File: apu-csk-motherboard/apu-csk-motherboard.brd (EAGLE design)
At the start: 90.2 x 95.9 mm, 11 parts

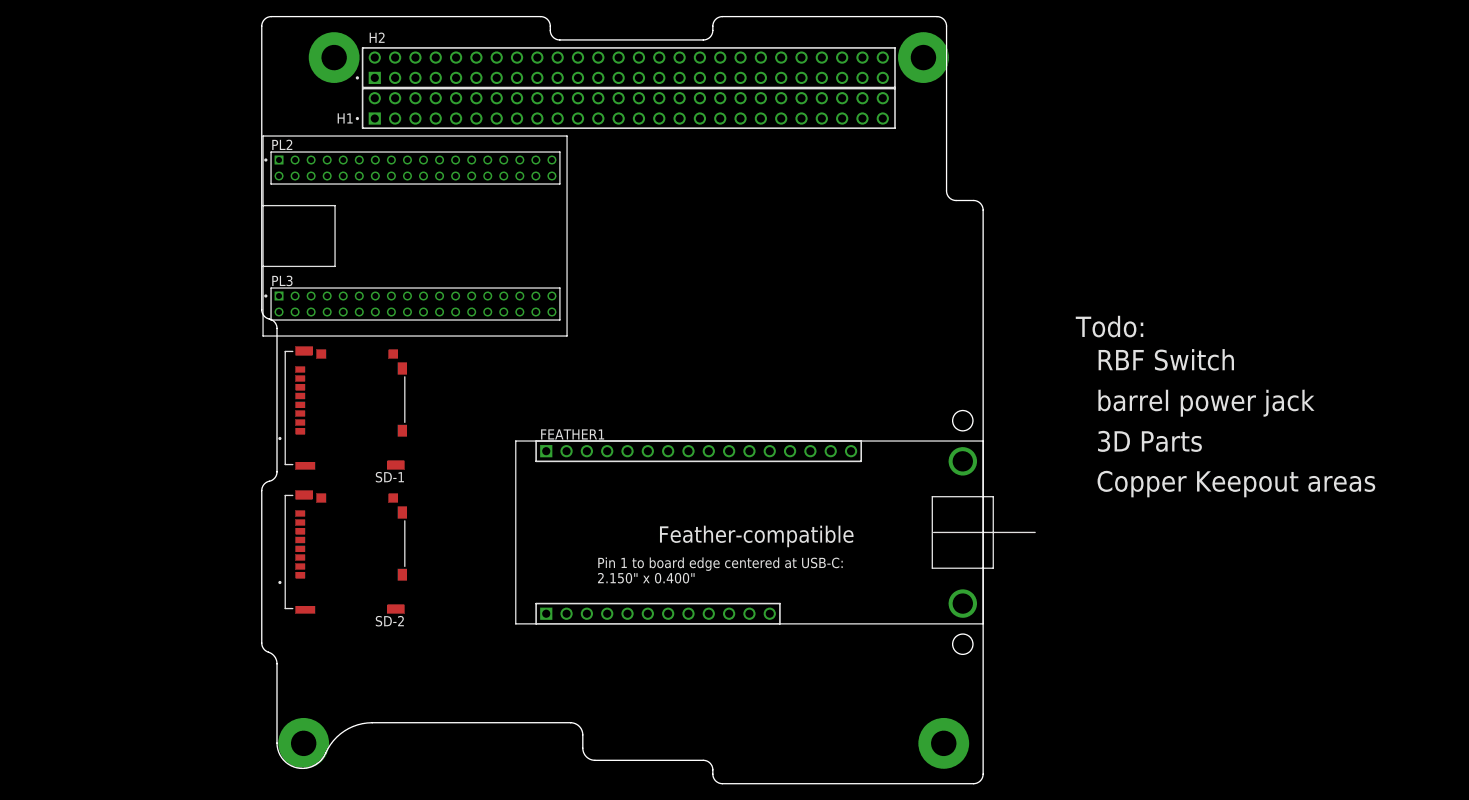
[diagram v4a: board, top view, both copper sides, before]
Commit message: Added 4 temperature sensors, Authenitcation Chip, and Conncetors for RBF Switch
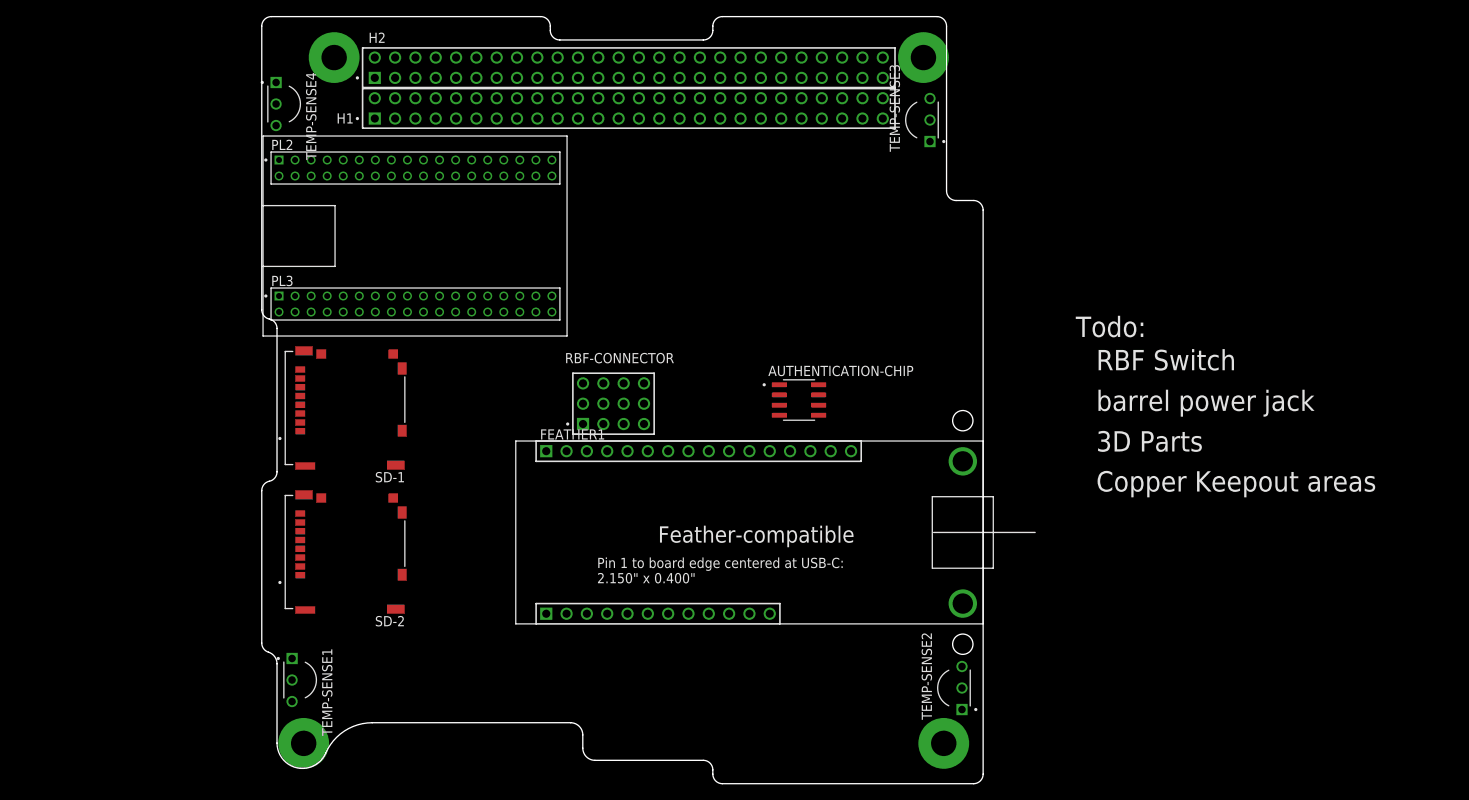
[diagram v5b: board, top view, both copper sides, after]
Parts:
- added AUTHENTICATION-CHIP: ATECC608A-SSHDA-B, ATECC608A-SSHDA-B:SOIC127P600X175-8N
- added RBF-CONNECTOR: TSW-104-05-G-T, TSW-104-05-G-T:SAMTEC_TSW-104-05-G-T
- added TEMP-SENSE1, TEMP-SENSE2, TEMP-SENSE3, TEMP-SENSE4: DS18B20, DS18B20:TO92269P495H695-3
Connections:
- new net DQ-TEMP: FEATHER1.T8, H2.16, TEMP-SENSE1.2, TEMP-SENSE2.2, TEMP-SENSE3.2, TEMP-SENSE4.2
- net 3.3V: now also AUTHENTICATION-CHIP.8, TEMP-SENSE1.3, TEMP-SENSE2.3, TEMP-SENSE3.3, TEMP-SENSE4.3
- net GND: now also AUTHENTICATION-CHIP.4, TEMP-SENSE1.1, TEMP-SENSE2.1, TEMP-SENSE3.1, TEMP-SENSE4.1

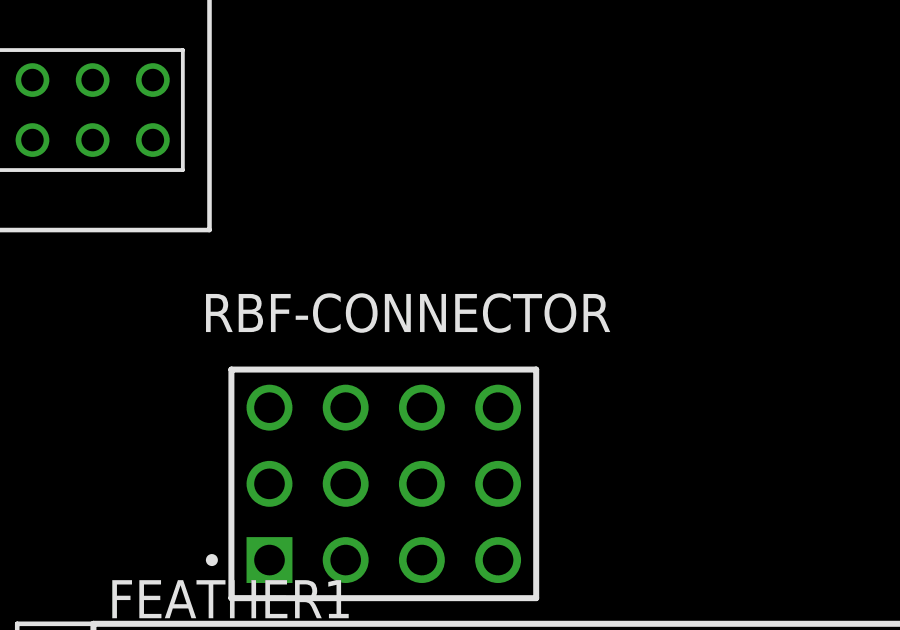
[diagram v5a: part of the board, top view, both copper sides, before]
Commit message: Added the components to a second sheet and finished wiring the authenticator chip
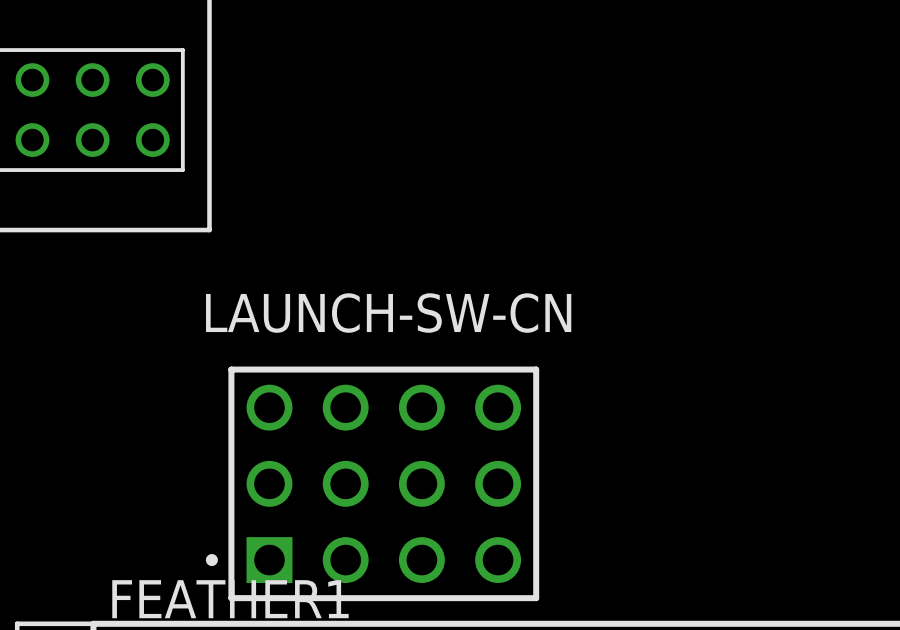
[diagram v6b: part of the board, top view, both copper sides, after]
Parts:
- renumbered RBF-CONNECTOR to LAUNCH-SW-CN
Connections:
- net CS-1 renamed CS-SD-1
- net CS-2 renamed CS-SD-2
- new net LSW-1-C: LAUNCH-SW-CN.03
- new net LSW-1-NC: LAUNCH-SW-CN.01
- new net LSW-1-NO: LAUNCH-SW-CN.02
- new net LSW-2-C: LAUNCH-SW-CN.06
- new net LSW-2-NC: LAUNCH-SW-CN.04
- new net LSW-2-NO: LAUNCH-SW-CN.05
- new net LSW-3-C: LAUNCH-SW-CN.09
- new net LSW-3-NC: LAUNCH-SW-CN.07
- new net LSW-3-NO: LAUNCH-SW-CN.08
- new net LSW-4-C: LAUNCH-SW-CN.12
- new net LSW-4-NC: LAUNCH-SW-CN.10
- new net LSW-4-NO: LAUNCH-SW-CN.11
- net CS-SD: no longer FEATHER1.T10
- net SCL: now also AUTHENTICATION-CHIP.6
- net SDA: now also AUTHENTICATION-CHIP.5
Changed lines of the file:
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@@
 <attribute name="VALUE" x="63.15" y="45" size="1.27" layer="27" align="top-left"/>
 </element>
-<element name="RBF-CONNECTOR" library="TSW-104-05-G-T" package="SAMTEC_TSW-104-05-G-T" value="TSW-104-05-G-T" x="40" y="45" smashed="yes">
+<element name="LAUNCH-SW-CN" library="TSW-104-05-G-T" package="SAMTEC_TSW-104-05-G-T" value="TSW-104-05-G-T" x="40" y="45" smashed="yes">
 <attribute name="MANUFACTURER" value="Samtec" x="40" y="45" size="1.778" layer="27" display="off"/>
 <attribute name="NAME" x="37.73" y="52.6" size="1.27" layer="25"/>
@@
 <contactref element="FEATHER1" pad="B1"/>
 <contactref element="H1" pad="41"/>
-<wire x1="35.4009" y1="21.2852" x2="64.77" y2="83.185" width="0" layer="19" extent="1-1"/>
+<contactref element="AUTHENTICATION-CHIP" pad="5"/>
+<wire x1="69.455" y1="46.095" x2="64.77" y2="83.185" width="0" layer="19" extent="1-1"/>
+<wire x1="35.4009" y1="21.2852" x2="69.455" y2="46.095" width="0" layer="19" extent="1-1"/>
 </signal>
 <signal name="SCL">
 <contactref element="FEATHER1" pad="B2"/>
 <contactref element="H1" pad="43"/>
-<wire x1="37.9409" y1="21.2852" x2="67.31" y2="83.185" width="0" layer="19" extent="1-1"/>
+<contactref element="AUTHENTICATION-CHIP" pad="6"/>
+<wire x1="69.455" y1="47.365" x2="67.31" y2="83.185" width="0" layer="19" extent="1-1"/>
+<wire x1="37.9409" y1="21.2852" x2="69.455" y2="47.365" width="0" layer="19" extent="1-1"/>
 </signal>
 <signal name="USER0">
@@
 <contactref element="H1" pad="17"/>
 </signal>
-<signal name="CS-1">
-<contactref element="SD-1" pad="2"/>
-<contactref element="FEATHER1" pad="T12"/>
-<wire x1="4.645" y1="45.2" x2="63.3409" y2="41.6052" width="0" layer="19" extent="1-1"/>
-</signal>
-<signal name="CS-2">
-<contactref element="SD-2" pad="2"/>
-<contactref element="FEATHER1" pad="T11"/>
-<wire x1="4.645" y1="27.2" x2="60.8009" y2="41.6052" width="0" layer="19" extent="1-1"/>
-</signal>
 <signal name="COPI">
 <contactref element="SD-2" pad="3"/>
@@
 </signal>
 <signal name="CS-SD">
-<contactref element="FEATHER1" pad="T10"/>
 <contactref element="H1" pad="24"/>
-<wire x1="58.2609" y1="41.6052" x2="41.91" y2="85.725" width="0" layer="19" extent="1-1"/>
 </signal>
 <signal name="UC_RXO">
@@
 <wire x1="1.63" y1="85" x2="83.37" y2="83" width="0" layer="19" extent="1-1"/>
 </signal>
+<signal name="CS-SD-2">
+<contactref element="SD-2" pad="2"/>
+<contactref element="FEATHER1" pad="T11"/>
+<wire x1="4.645" y1="27.2" x2="60.8009" y2="41.6052" width="0" layer="19" extent="1-1"/>
+</signal>
+<signal name="CS-SD-1">
+<contactref element="SD-1" pad="2"/>
+<contactref element="FEATHER1" pad="T12"/>
+<wire x1="4.645" y1="45.2" x2="63.3409" y2="41.6052" width="0" layer="19" extent="1-1"/>
+</signal>
+<signal name="LSW-1-NO">
+<contactref element="LAUNCH-SW-CN" pad="02"/>
+</signal>
+<signal name="LSW-2-NO">
+<contactref element="LAUNCH-SW-CN" pad="05"/>
+</signal>
+<signal name="LSW-3-NO">
+<contactref element="LAUNCH-SW-CN" pad="08"/>
+</signal>
+<signal name="LSW-4-NO">
+<contactref element="LAUNCH-SW-CN" pad="11"/>
+</signal>
+<signal name="LSW-1-C">
+<contactref element="LAUNCH-SW-CN" pad="03"/>
+</signal>
+<signal name="LSW-2-C">
+<contactref element="LAUNCH-SW-CN" pad="06"/>
+</signal>
+<signal name="LSW-3-C">
+<contactref element="LAUNCH-SW-CN" pad="09"/>
+</signal>
+<signal name="LSW-4-C">
+<contactref element="LAUNCH-SW-CN" pad="12"/>
+</signal>
+<signal name="LSW-4-NC">
+<contactref element="LAUNCH-SW-CN" pad="10"/>
+</signal>
+<signal name="LSW-3-NC">
+<contactref element="LAUNCH-SW-CN" pad="07"/>
+</signal>
+<signal name="LSW-2-NC">
+<contactref element="LAUNCH-SW-CN" pad="04"/>
+</signal>
+<signal name="LSW-1-NC">
+<contactref element="LAUNCH-SW-CN" pad="01"/>
+</signal>
 </signals>

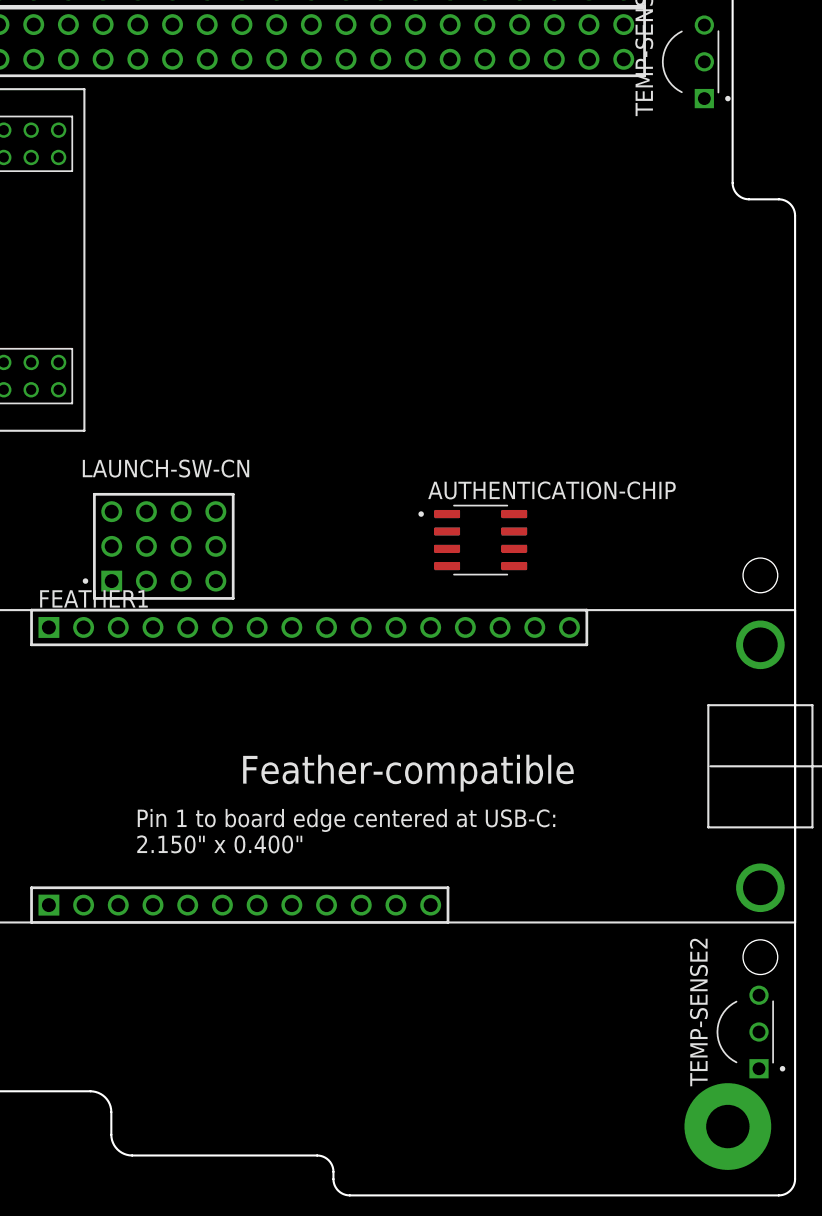
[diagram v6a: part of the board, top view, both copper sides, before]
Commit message: Added FRAM and RTC but need to finish connections
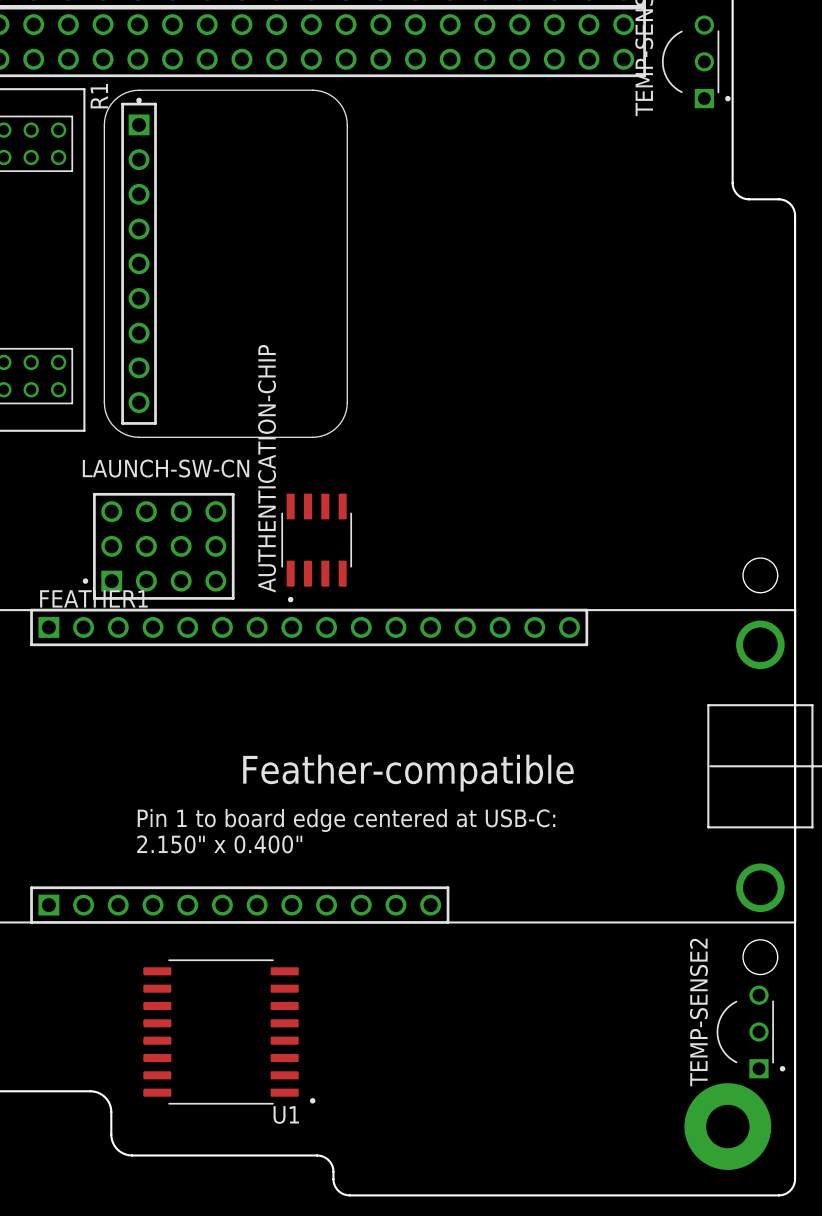
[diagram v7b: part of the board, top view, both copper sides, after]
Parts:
- added R1: FRAM_ADAFRUIT_MB85RSMT, apu-csk-motherboard:FRAM_ADAFRUIT_MB85RSMT
- added U1: DS3231M+TRL, DS3231M_TRL:SOIC127P1032X265-16N
- moved AUTHENTICATION-CHIP 12.0 mm to (55.0, 48.0), turned to 90 degrees
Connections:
- new net CS-FRAM: FEATHER1.T10, R1.07
- new net N$11: U1.3
- new net N$6: U1.14
- new net N$9: U1.4
- new net RTCLOCK: U1.1
- new net WP-FRAM: FEATHER1.B3, R1.08
- net 3.3V: now also R1.01, U1.2
- net CIPO: now also R1.05
- net COPI: now also R1.06
- net GND: now also R1.03, U1.13
- net SCK: now also R1.04
- net SCL: now also U1.16
- net SDA: now also U1.15
